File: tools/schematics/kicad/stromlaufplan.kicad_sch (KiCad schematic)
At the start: 4 parts, among them K1 Relaismodul (6 Kanaele), U1 MCP23017, U2 I2C Level-Shifter (4-Kanal, b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

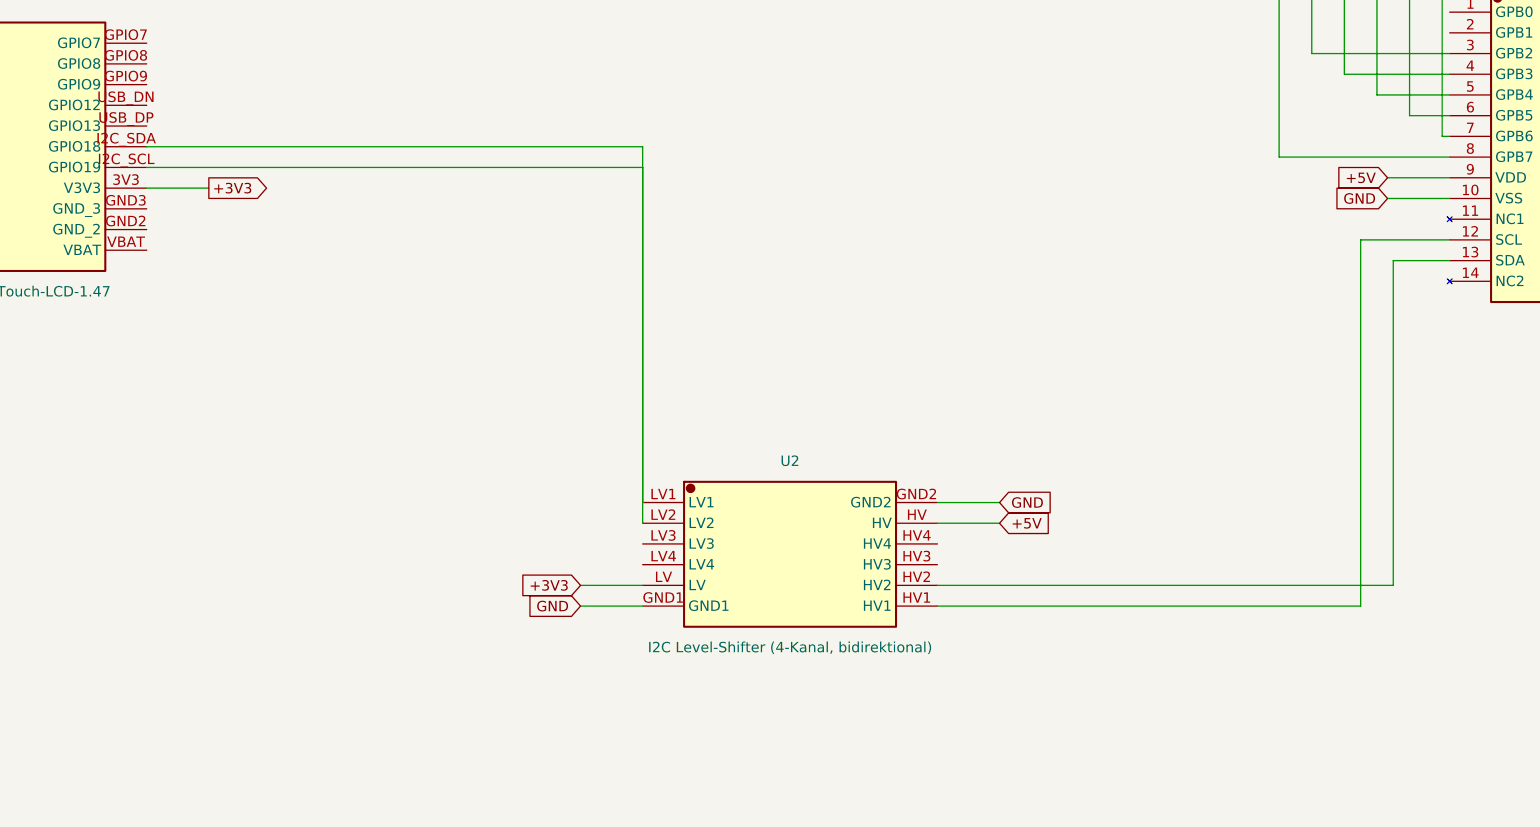
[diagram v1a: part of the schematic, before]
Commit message: Schematics: Level-Shifter-Symbol auf physisches Modul-Pinout umgestellt
Pins jetzt oben/unten statt links/rechts, passend zum Foto des
4-Kanal-Moduls: oben HV1 HV2 HV GND HV3 HV4, unten LV1 LV2 LV GND LV3
LV4 (je zwei GND-Pads als eigener Anker, aber mit gleichem "GND"-Label
angezeigt). IcDef unterstuetzt jetzt zusaetzlich zu links/rechts auch
oben/unten-Pins fuer Header-/Modul-artige Bauteile.

Co-Authored-By: Claude Sonnet 5 <noreply@anthropic.com>
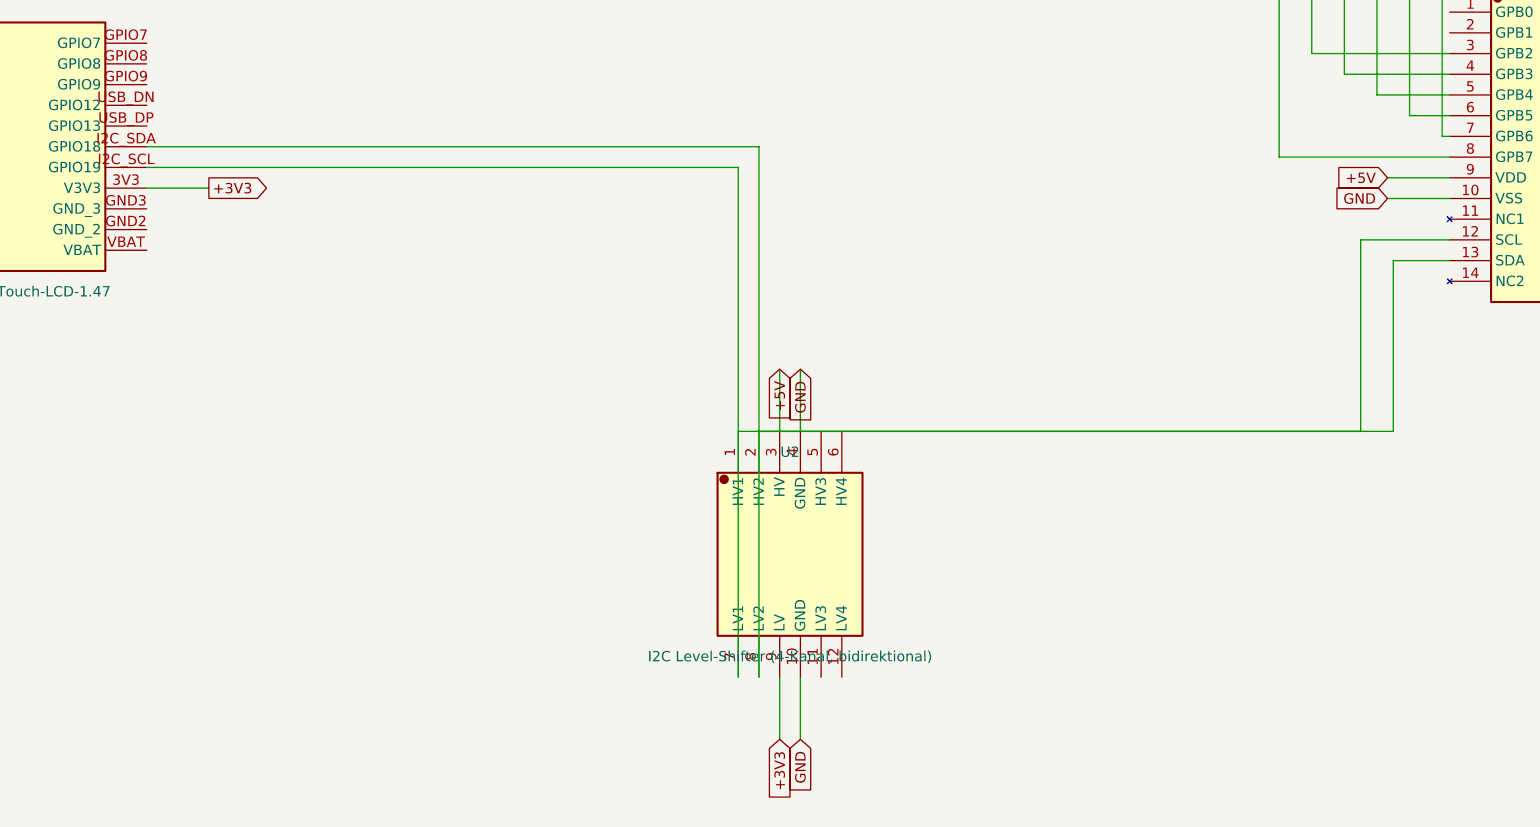
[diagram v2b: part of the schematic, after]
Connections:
- net +3V3: now also U2.9 (LV); no longer U2.LV
- net +5V: now also U2.3 (HV); no longer U2.HV
- net GND: now also U2.10 (GND), U2.4 (GND); no longer U2.GND1, U2.GND2
- net at U1.12 (SCL): now also U1.13 (SDA), U2.1 (HV1), U2.2 (HV2); no longer U2.HV1
- new net: A1.I2C_SCL (GPIO19), U2.7 (LV1)
- new net: A1.I2C_SDA (GPIO18), U2.8 (LV2)
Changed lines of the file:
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@@
 		(unit 1)
 		(in_bom yes) (on_board yes) (dnp no)
-		(property "Reference" "U2" (at 160.00 188.57 0) (effects (font (size 1.27 1.27))))
-		(property "Value" "I2C Level-Shifter (4-Kanal, bidirektional)" (at 160.00 211.43 0) (effects (font (size 1.27 1.27))))
-		(pin "LV1")
-		(pin "LV2")
-		(pin "LV3")
-		(pin "LV4")
-		(pin "LV")
-		(pin "GND1")
-		(pin "GND2")
-		(pin "HV")
-		(pin "HV4")
-		(pin "HV3")
-		(pin "HV2")
-		(pin "HV1")
+		(property "Reference" "U2" (at 160.00 187.46 0) (effects (font (size 1.27 1.27))))
+		(property "Value" "I2C Level-Shifter (4-Kanal, bidirektional)" (at 160.00 212.54 0) (effects (font (size 1.27 1.27))))
+		(pin "1")
+		(pin "2")
+		(pin "3")
+		(pin "4")
+		(pin "5")
+		(pin "6")
+		(pin "7")
+		(pin "8")
+		(pin "9")
+		(pin "10")
+		(pin "11")
+		(pin "12")
 	)
-	(wire (pts (xy 81.08 152.54) (xy 141.92 152.54)) (stroke (width 0.1524) (type default)))
-	(wire (pts (xy 141.92 152.54) (xy 141.92 193.65)) (stroke (width 0.1524) (type default)))
-	(wire (pts (xy 81.08 150.00) (xy 141.92 150.00)) (stroke (width 0.1524) (type default)))
-	(wire (pts (xy 141.92 150.00) (xy 141.92 196.19)) (stroke (width 0.1524) (type default)))
-	(wire (pts (xy 178.08 206.35) (xy 230.00 206.35)) (stroke (width 0.1524) (type default)))
-	(wire (pts (xy 230.00 206.35) (xy 230.00 161.43)) (stroke (width 0.1524) (type default)))
+	(wire (pts (xy 81.08 152.54) (xy 153.65 152.54)) (stroke (width 0.1524) (type default)))
+	(wire (pts (xy 153.65 152.54) (xy 153.65 215.08)) (stroke (width 0.1524) (type default)))
+	(wire (pts (xy 81.08 150.00) (xy 156.19 150.00)) (stroke (width 0.1524) (type default)))
+	(wire (pts (xy 156.19 150.00) (xy 156.19 215.08)) (stroke (width 0.1524) (type default)))
+	(wire (pts (xy 153.65 184.92) (xy 230.00 184.92)) (stroke (width 0.1524) (type default)))
+	(wire (pts (xy 230.00 184.92) (xy 230.00 161.43)) (stroke (width 0.1524) (type default)))
 	(wire (pts (xy 230.00 161.43) (xy 240.92 161.43)) (stroke (width 0.1524) (type default)))
-	(wire (pts (xy 178.08 203.81) (xy 234.00 203.81)) (stroke (width 0.1524) (type default)))
-	(wire (pts (xy 234.00 203.81) (xy 234.00 163.97)) (stroke (width 0.1524) (type default)))
+	(wire (pts (xy 156.19 184.92) (xy 234.00 184.92)) (stroke (width 0.1524) (type default)))
+	(wire (pts (xy 234.00 184.92) (xy 234.00 163.97)) (stroke (width 0.1524) (type default)))
 	(wire (pts (xy 234.00 163.97) (xy 240.92 163.97)) (stroke (width 0.1524) (type default)))
 	(wire (pts (xy 240.92 151.27) (xy 220.00 151.27)) (stroke (width 0.1524) (type default)))
@@
 		(effects (font (size 1.27 1.27)) (justify right))
 	)
-	(wire (pts (xy 141.92 203.81) (xy 134.30 203.81)) (stroke (width 0.1524) (type default)))
-	(global_label "+3V3" (shape input) (at 134.30 203.81 180)
+	(wire (pts (xy 158.73 215.08) (xy 158.73 222.70)) (stroke (width 0.1524) (type default)))
+	(global_label "+3V3" (shape input) (at 158.73 222.70 270)
 		(effects (font (size 1.27 1.27)) (justify right))
 	)
-	(wire (pts (xy 141.92 206.35) (xy 134.30 206.35)) (stroke (width 0.1524) (type default)))
-	(global_label "GND" (shape input) (at 134.30 206.35 180)
+	(wire (pts (xy 161.27 215.08) (xy 161.27 222.70)) (stroke (width 0.1524) (type default)))
+	(global_label "GND" (shape input) (at 161.27 222.70 270)
 		(effects (font (size 1.27 1.27)) (justify right))
 	)
-	(wire (pts (xy 178.08 196.19) (xy 185.70 196.19)) (stroke (width 0.1524) (type default)))
-	(global_label "+5V" (shape input) (at 185.70 196.19 0)
-		(effects (font (size 1.27 1.27)) (justify left))
+	(wire (pts (xy 158.73 184.92) (xy 158.73 177.30)) (stroke (width 0.1524) (type default)))
+	(global_label "+5V" (shape input) (at 158.73 177.30 90)
+		(effects (font (size 1.27 1.27)) (justify right))
 	)
-	(wire (pts (xy 178.08 193.65) (xy 185.70 193.65)) (stroke (width 0.1524) (type default)))
-	(global_label "GND" (shape input) (at 185.70 193.65 0)
-		(effects (font (size 1.27 1.27)) (justify left))
+	(wire (pts (xy 161.27 184.92) (xy 161.27 177.30)) (stroke (width 0.1524) (type default)))
+	(global_label "GND" (shape input) (at 161.27 177.30 90)
+		(effects (font (size 1.27 1.27)) (justify right))
 	)
 	(wire (pts (xy 240.92 153.81) (xy 233.30 153.81)) (stroke (width 0.1524) (type default)))

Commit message: Schematics: ESP32/Relay-Pinreihenfolge 1:1 nach Waveshare-Pinout (kein DIP-Wrap)
Die DIP/SOIC-Wraparound-Nummerierung (rechte Spalte umgekehrt) galt
bisher pauschal fuer alle vier Bauteile -- korrekt nur fuer echte
DIP-Chips wie den MCP23017. ESP32-Board und Relaismodul sind einfache
2-reihige Pinheader ohne Wraparound: rechte Spalte liest jetzt wie im
offiziellen Waveshare-Pinout-Bild einfach oben-nach-unten, genau wie
die linke. IcDef.dip_wrap steuert das jetzt pro Bauteil.

Co-Authored-By: Claude Sonnet 5 <noreply@anthropic.com>
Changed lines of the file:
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@@
 		(pin "GPIO5")
 		(pin "GPIO6")
+		(pin "VBAT")
+		(pin "GND2")
+		(pin "GND3")
+		(pin "3V3")
+		(pin "I2C_SCL")
+		(pin "I2C_SDA")
+		(pin "USB_DP")
+		(pin "USB_DN")
+		(pin "GPIO9")
+		(pin "GPIO8")
 		(pin "GPIO7")
-		(pin "GPIO8")
-		(pin "GPIO9")
-		(pin "USB_DN")
-		(pin "USB_DP")
-		(pin "I2C_SDA")
-		(pin "I2C_SCL")
-		(pin "3V3")
-		(pin "GND3")
-		(pin "GND2")
-		(pin "VBAT")
 	)
 	(symbol
@@
 		(pin "OUT4")
 		(pin "OUT5")
+		(pin "IN0")
+		(pin "IN1")
+		(pin "IN2")
+		(pin "IN3")
+		(pin "IN4")
 		(pin "IN5")
-		(pin "IN4")
-		(pin "IN3")
-		(pin "IN2")
-		(pin "IN1")
-		(pin "IN0")
 	)
 	(symbol
@@
 		(pin "12")
 	)
-	(wire (pts (xy 81.08 152.54) (xy 153.65 152.54)) (stroke (width 0.1524) (type default)))
-	(wire (pts (xy 153.65 152.54) (xy 153.65 215.08)) (stroke (width 0.1524) (type default)))
+	(wire (pts (xy 81.08 147.46) (xy 153.65 147.46)) (stroke (width 0.1524) (type default)))
+	(wire (pts (xy 153.65 147.46) (xy 153.65 215.08)) (stroke (width 0.1524) (type default)))
 	(wire (pts (xy 81.08 150.00) (xy 156.19 150.00)) (stroke (width 0.1524) (type default)))
 	(wire (pts (xy 156.19 150.00) (xy 156.19 215.08)) (stroke (width 0.1524) (type default)))
@@
 	(wire (pts (xy 234.00 163.97) (xy 240.92 163.97)) (stroke (width 0.1524) (type default)))
 	(wire (pts (xy 240.92 151.27) (xy 220.00 151.27)) (stroke (width 0.1524) (type default)))
-	(wire (pts (xy 220.00 151.27) (xy 220.00 66.35)) (stroke (width 0.1524) (type default)))
-	(wire (pts (xy 220.00 66.35) (xy 188.08 66.35)) (stroke (width 0.1524) (type default)))
+	(wire (pts (xy 220.00 151.27) (xy 220.00 53.65)) (stroke (width 0.1524) (type default)))
+	(wire (pts (xy 220.00 53.65) (xy 188.08 53.65)) (stroke (width 0.1524) (type default)))
 	(wire (pts (xy 240.92 138.57) (xy 224.00 138.57)) (stroke (width 0.1524) (type default)))
-	(wire (pts (xy 224.00 138.57) (xy 224.00 63.81)) (stroke (width 0.1524) (type default)))
-	(wire (pts (xy 224.00 63.81) (xy 188.08 63.81)) (stroke (width 0.1524) (type default)))
+	(wire (pts (xy 224.00 138.57) (xy 224.00 56.19)) (stroke (width 0.1524) (type default)))
+	(wire (pts (xy 224.00 56.19) (xy 188.08 56.19)) (stroke (width 0.1524) (type default)))
 	(wire (pts (xy 240.92 141.11) (xy 228.00 141.11)) (stroke (width 0.1524) (type default)))
-	(wire (pts (xy 228.00 141.11) (xy 228.00 61.27)) (stroke (width 0.1524) (type default)))
-	(wire (pts (xy 228.00 61.27) (xy 188.08 61.27)) (stroke (width 0.1524) (type default)))
+	(wire (pts (xy 228.00 141.11) (xy 228.00 58.73)) (stroke (width 0.1524) (type default)))
+	(wire (pts (xy 228.00 58.73) (xy 188.08 58.73)) (stroke (width 0.1524) (type default)))
 	(wire (pts (xy 240.92 143.65) (xy 232.00 143.65)) (stroke (width 0.1524) (type default)))
-	(wire (pts (xy 232.00 143.65) (xy 232.00 58.73)) (stroke (width 0.1524) (type default)))
-	(wire (pts (xy 232.00 58.73) (xy 188.08 58.73)) (stroke (width 0.1524) (type default)))
+	(wire (pts (xy 232.00 143.65) (xy 232.00 61.27)) (stroke (width 0.1524) (type default)))
+	(wire (pts (xy 232.00 61.27) (xy 188.08 61.27)) (stroke (width 0.1524) (type default)))
 	(wire (pts (xy 240.92 146.19) (xy 236.00 146.19)) (stroke (width 0.1524) (type default)))
-	(wire (pts (xy 236.00 146.19) (xy 236.00 56.19)) (stroke (width 0.1524) (type default)))
-	(wire (pts (xy 236.00 56.19) (xy 188.08 56.19)) (stroke (width 0.1524) (type default)))
+	(wire (pts (xy 236.00 146.19) (xy 236.00 63.81)) (stroke (width 0.1524) (type default)))
+	(wire (pts (xy 236.00 63.81) (xy 188.08 63.81)) (stroke (width 0.1524) (type default)))
 	(wire (pts (xy 240.92 148.73) (xy 240.00 148.73)) (stroke (width 0.1524) (type default)))
-	(wire (pts (xy 240.00 148.73) (xy 240.00 53.65)) (stroke (width 0.1524) (type default)))
-	(wire (pts (xy 240.00 53.65) (xy 188.08 53.65)) (stroke (width 0.1524) (type default)))
+	(wire (pts (xy 240.00 148.73) (xy 240.00 66.35)) (stroke (width 0.1524) (type default)))
+	(wire (pts (xy 240.00 66.35) (xy 188.08 66.35)) (stroke (width 0.1524) (type default)))
 	(wire (pts (xy 38.92 137.30) (xy 31.30 137.30)) (stroke (width 0.1524) (type default)))
 	(global_label "+5V" (shape output) (at 31.30 137.30 180)
 		(effects (font (size 1.27 1.27)) (justify right))
 	)
-	(wire (pts (xy 81.08 155.08) (xy 88.70 155.08)) (stroke (width 0.1524) (type default)))
-	(global_label "+3V3" (shape output) (at 88.70 155.08 0)
+	(wire (pts (xy 81.08 144.92) (xy 88.70 144.92)) (stroke (width 0.1524) (type default)))
+	(global_label "+3V3" (shape output) (at 88.70 144.92 0)
 		(effects (font (size 1.27 1.27)) (justify left))
 	)

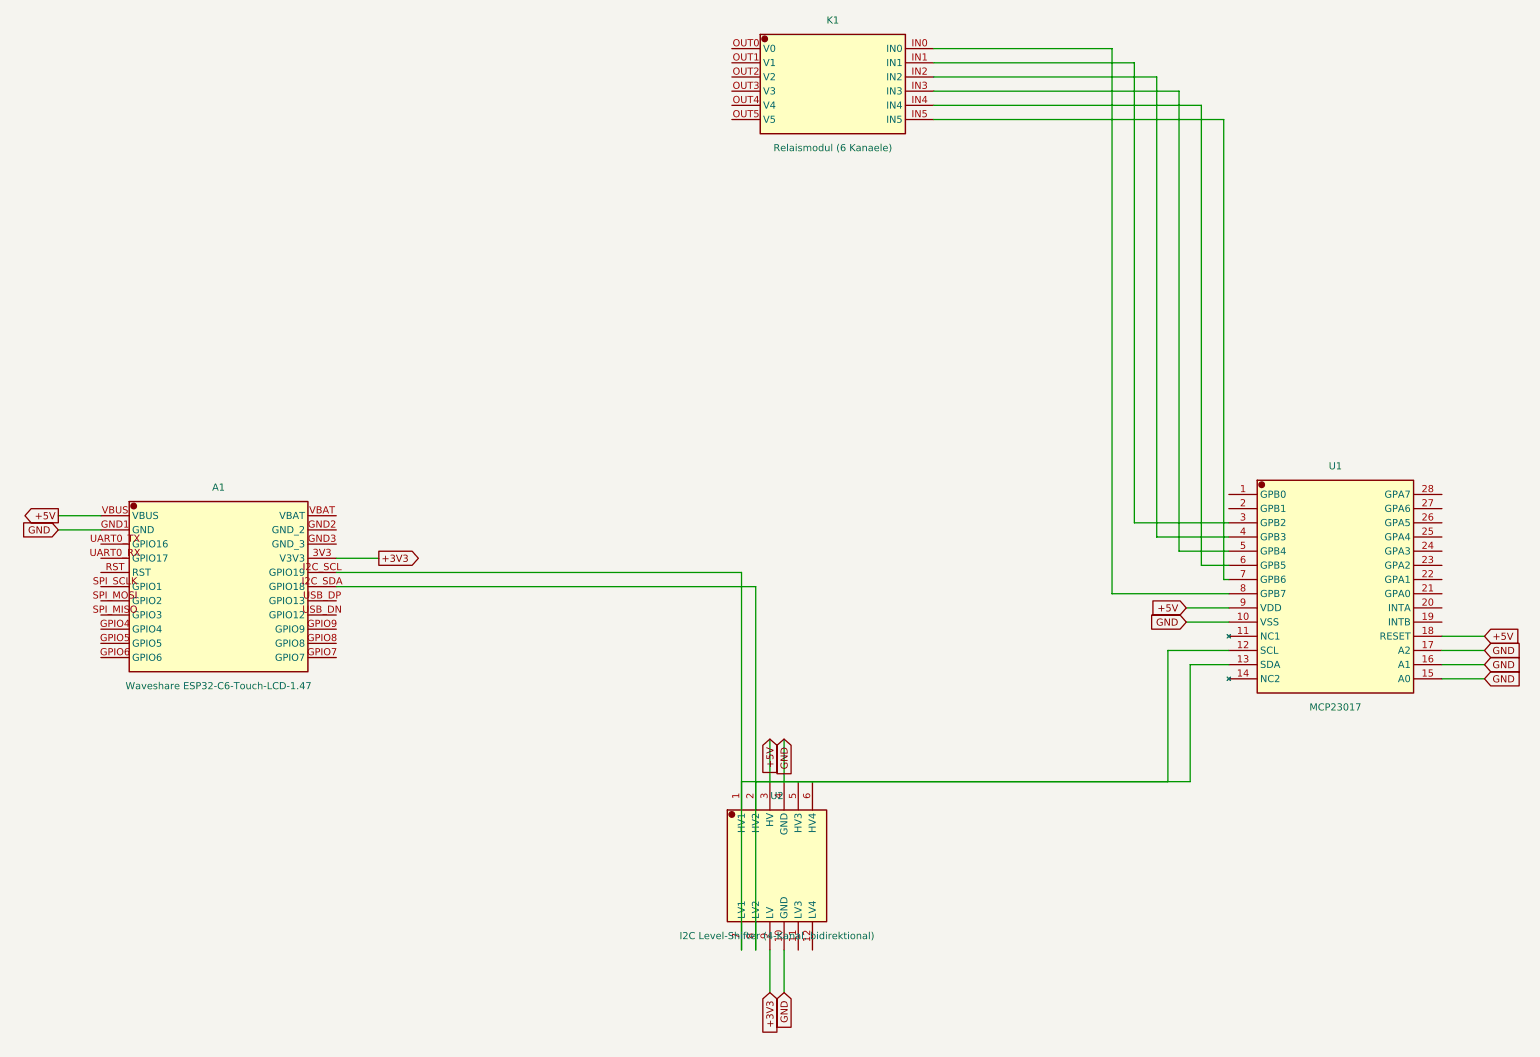
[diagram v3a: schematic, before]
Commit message: Schematics: KiCad-Pins auf sauberes Raster ausgerichtet
Ursache fuer "Verbindung laesst sich nicht herstellen": Pin-Positionen
lagen bei geradzahligen Pin-Anzahlen (MCP23017, Relais) und beim
oben/unten-Layout des Level-Shifters teils einen halben Rasterschritt
daneben, dazu einige Platzierungs-/Wire-Koordinaten nicht auf dem
2,54mm-Pitch-Raster. Der Cursor konnte dadurch nie exakt auf den Pin
schnappen. ERC-Warnungen "endpoint_off_grid": 45 -> 0.

Co-Authored-By: Claude Sonnet 5 <noreply@anthropic.com>
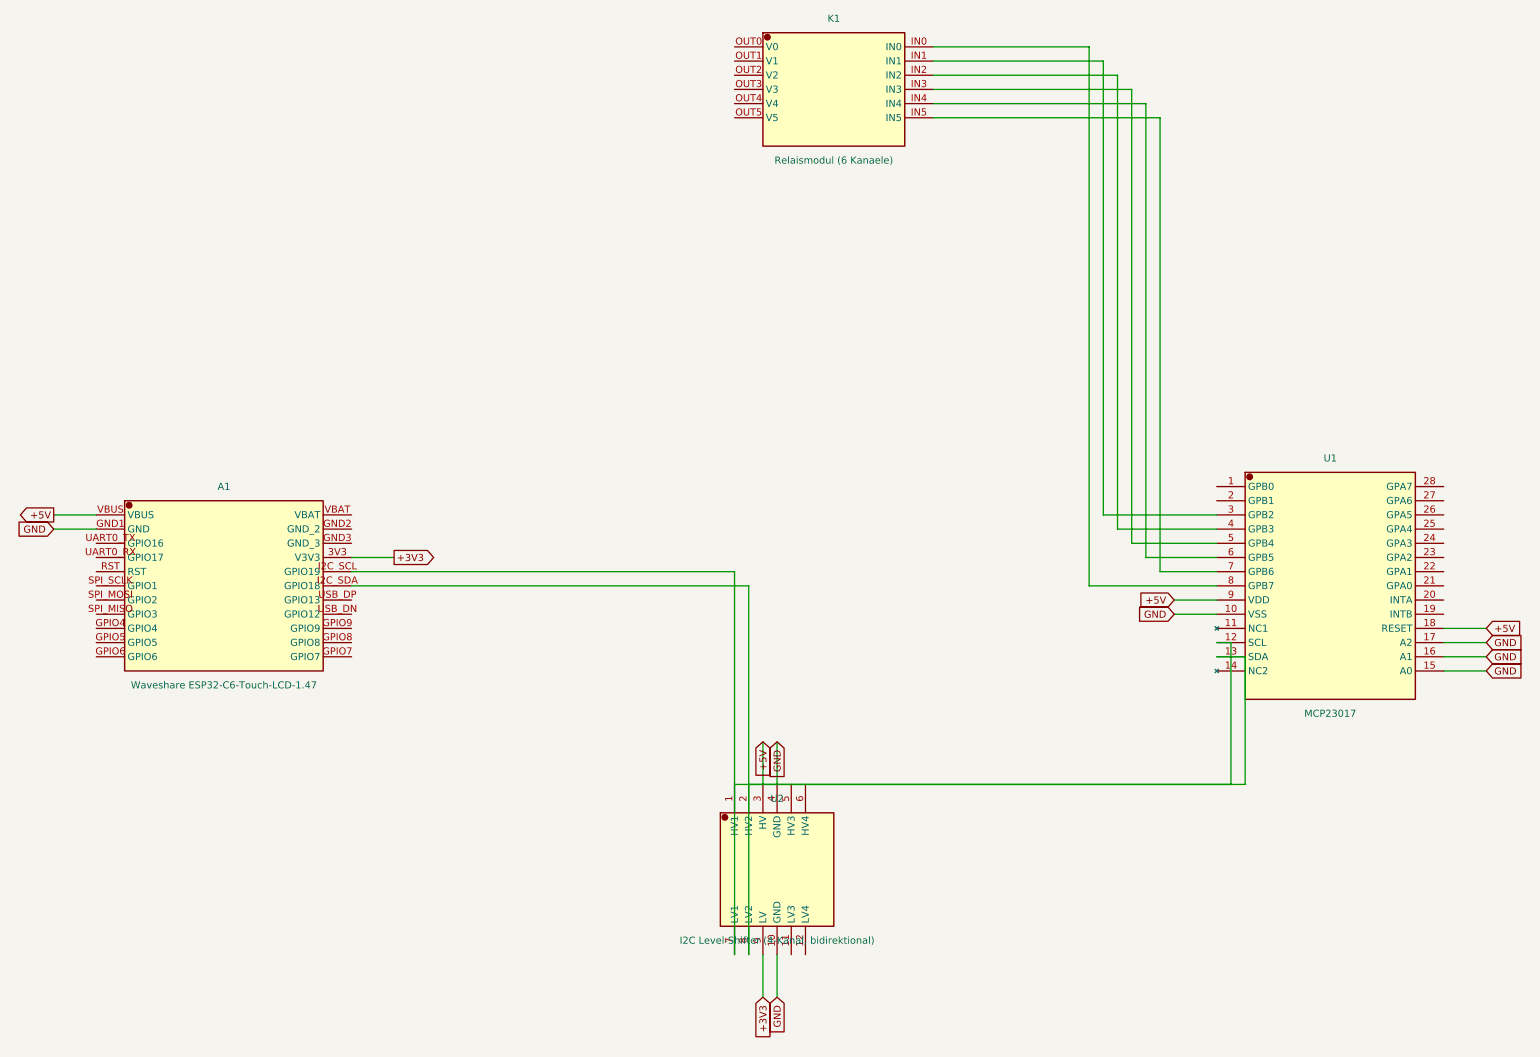
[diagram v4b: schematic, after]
